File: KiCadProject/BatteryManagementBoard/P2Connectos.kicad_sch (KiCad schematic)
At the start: 25 parts

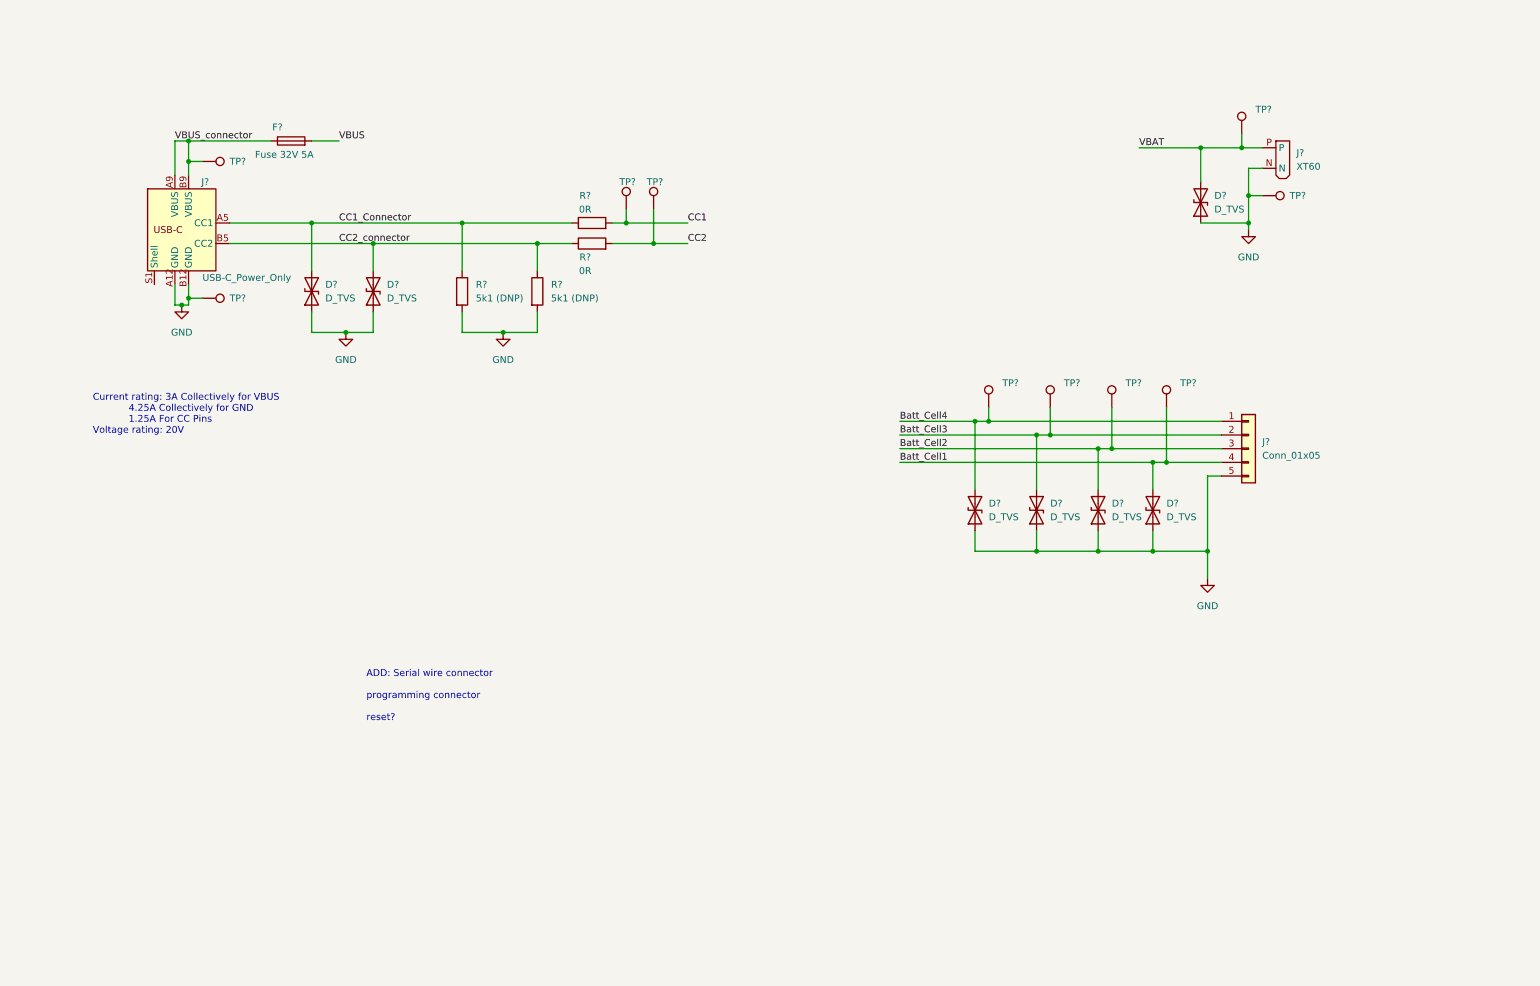
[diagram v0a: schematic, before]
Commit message: BQ25713 layout start
Signed-off-by: Eldalote.Electronics <Eldalote.Electronics@gmail.com>
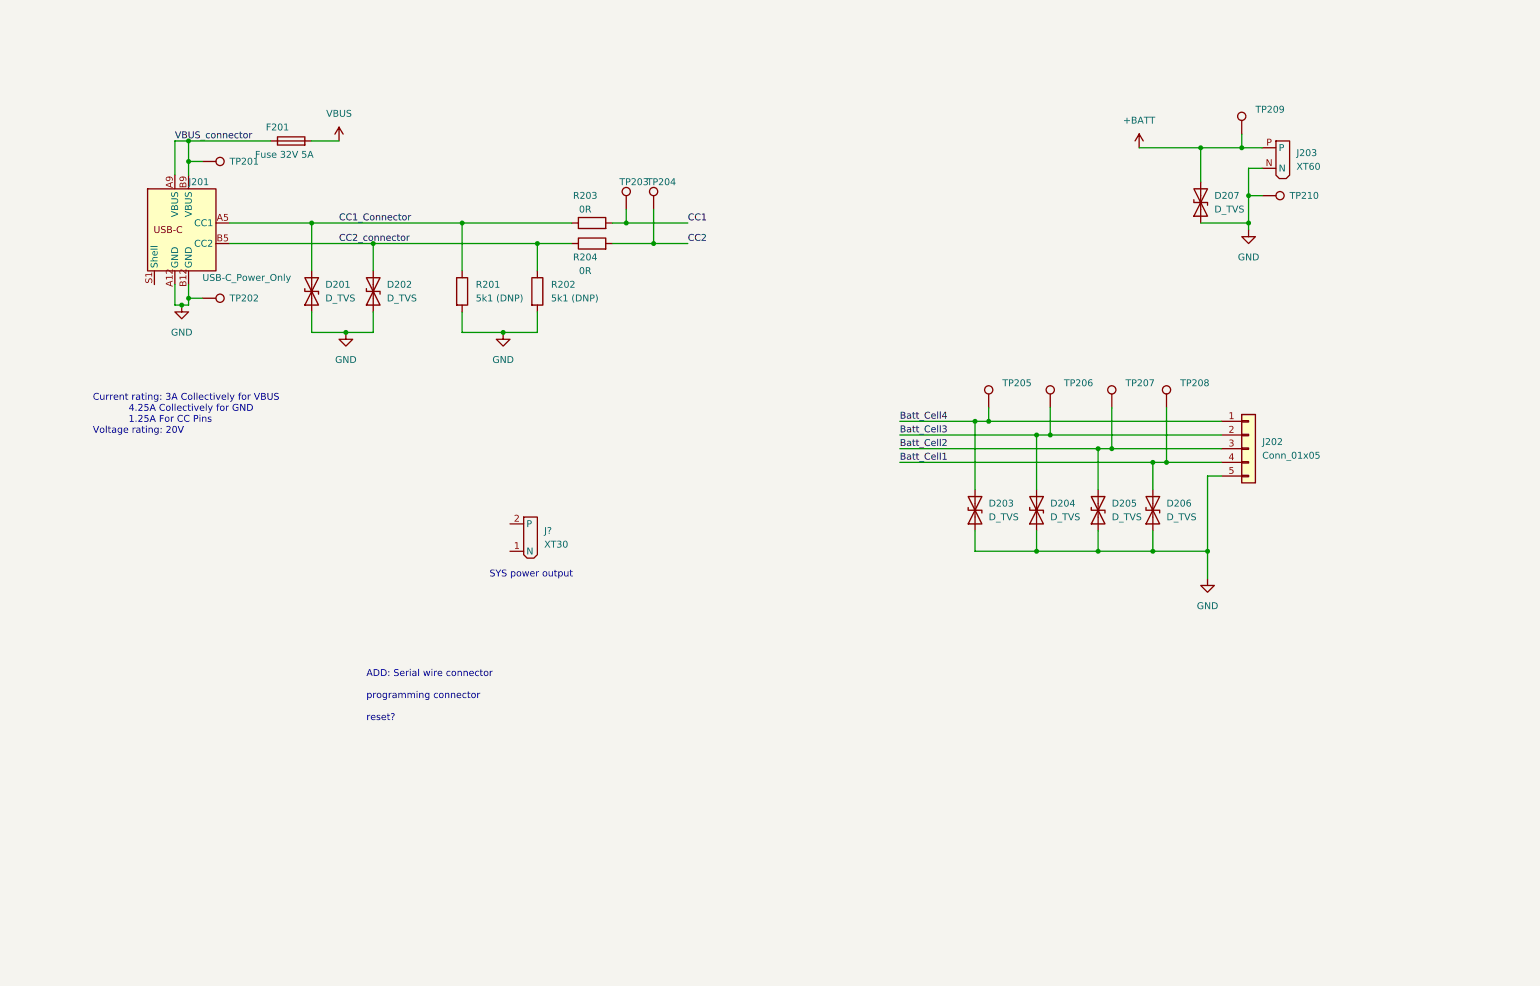
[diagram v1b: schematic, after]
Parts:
- added J?: XT30, Eldalote-footprints:XT30, symbol Eldalote_symbols:XT30
- gave numbers to parts that had none: 25
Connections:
- net VBAT renamed +BATT
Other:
- note added: "SYS power output"

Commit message: BQ25713 and LDO done? Stm32 next I think
Signed-off-by: Eldalote.Electronics <Eldalote.Electronics@gmail.com>
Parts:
- gave numbers to parts that had none: 1
- renumbered J202 to J203, J203 to J204
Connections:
- no-connect marks 0 -> 1
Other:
- note added: "ADD: Serial wire connector programming connector reset? Connector to ESP32"
- note added: "VOUT power output to LED driver"
- note removed: "ADD: Serial wire connector programming connector reset?"
- note removed: "SYS power output"
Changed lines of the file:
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@@
   (junction (at 194.31 91.44) (diameter 0) (color 0 0 0 0)
   )
+  (no_connect (at 39.37 66.04))
   (wire (pts (xy 217.17 88.9) (xy 217.17 96.52))
     (stroke (width 0) (type default) (color 0 0 0 0))
@@
     (stroke (width 0) (type default) (color 0 0 0 0))
   )
-  (text "SYS power output\n" (at 101.6 120.65 0)
-    (effects (font (size 1.27 1.27)) (justify left bottom))
-  )
-  (text "ADD: Serial wire connector\n\nprogramming connector\n\nreset?"
-    (at 78.74 147.32 0)
+  (text "VOUT power output to LED driver\n\n" (at 99.06 121.92 0)
+    (effects (font (size 1.27 1.27)) (justify left bottom))
+  )
+  (text "ADD: Serial wire connector\n\nprogramming connector\n\nreset?\n\nConnector to ESP32\n"
+    (at 55.88 152.4 0)
     (effects (font (size 1.27 1.27)) (justify left bottom))
   )
@@
   (symbol (lib_id "Eldalote_symbols:XT30") (at 107.95 113.03 0) (unit 1)
     (in_bom yes) (on_board yes) (fields_autoplaced)
-    (property "Reference" "J?" (id 0) (at 111.76 111.7599 0)
+    (property "Reference" "J202" (id 0) (at 111.76 111.7599 0)
       (effects (font (size 1.27 1.27)) (justify left))
     )
@@
   (symbol (lib_id "power:VBUS") (at 73.66 39.37 0) (unit 1)
     (in_bom yes) (on_board yes) (fields_autoplaced)
-    (property "Reference" "#PWR?" (id 0) (at 73.66 43.18 0)
+    (property "Reference" "#PWR0202" (id 0) (at 73.66 43.18 0)
       (effects (font (size 1.27 1.27)) hide)
     )
@@
   (symbol (lib_id "power:+BATT") (at 222.25 40.64 0) (unit 1)
     (in_bom yes) (on_board yes) (fields_autoplaced)
-    (property "Reference" "#PWR?" (id 0) (at 222.25 44.45 0)
+    (property "Reference" "#PWR0205" (id 0) (at 222.25 44.45 0)
       (effects (font (size 1.27 1.27)) hide)
     )
@@
   (symbol (lib_id "power:GND") (at 74.93 74.93 0) (unit 1)
     (in_bom yes) (on_board yes) (fields_autoplaced)
-    (property "Reference" "#PWR0202" (id 0) (at 74.93 81.28 0)
+    (property "Reference" "#PWR0203" (id 0) (at 74.93 81.28 0)
       (effects (font (size 1.27 1.27)) hide)
     )
@@
   (symbol (lib_id "Connector_Generic:Conn_01x05") (at 242.57 96.52 0) (unit 1)
     (in_bom yes) (on_board yes) (fields_autoplaced)
-    (property "Reference" "J202" (id 0) (at 245.11 95.2499 0)
+    (property "Reference" "J203" (id 0) (at 245.11 95.2499 0)
       (effects (font (size 1.27 1.27)) (justify left))
     )
@@
   (symbol (lib_id "power:GND") (at 234.95 120.65 0) (unit 1)
     (in_bom yes) (on_board yes) (fields_autoplaced)
-    (property "Reference" "#PWR0204" (id 0) (at 234.95 127 0)
+    (property "Reference" "#PWR0206" (id 0) (at 234.95 127 0)
       (effects (font (size 1.27 1.27)) hide)
     )
@@
   (symbol (lib_id "power:GND") (at 242.57 55.88 0) (unit 1)
     (in_bom yes) (on_board yes) (fields_autoplaced)
-    (property "Reference" "#PWR0205" (id 0) (at 242.57 62.23 0)
+    (property "Reference" "#PWR0207" (id 0) (at 242.57 62.23 0)
       (effects (font (size 1.27 1.27)) hide)
     )
@@
   (symbol (lib_id "power:GND") (at 104.14 74.93 0) (unit 1)
     (in_bom yes) (on_board yes) (fields_autoplaced)
-    (property "Reference" "#PWR0203" (id 0) (at 104.14 81.28 0)
+    (property "Reference" "#PWR0204" (id 0) (at 104.14 81.28 0)
       (effects (font (size 1.27 1.27)) hide)
     )
@@
   (symbol (lib_id "Eldalote_symbols:XT60") (at 247.65 43.18 0) (unit 1)
     (in_bom yes) (on_board yes) (fields_autoplaced)
-    (property "Reference" "J203" (id 0) (at 251.46 41.5924 0)
-      (effects (font (size 1.27 1.27)) (justify left))
-    )
+    (property "Reference" "J204" (id 0) (at 251.46 41.5924 0)
+      (effects (font (size 1.27 1.27)) (justify left))
+    )

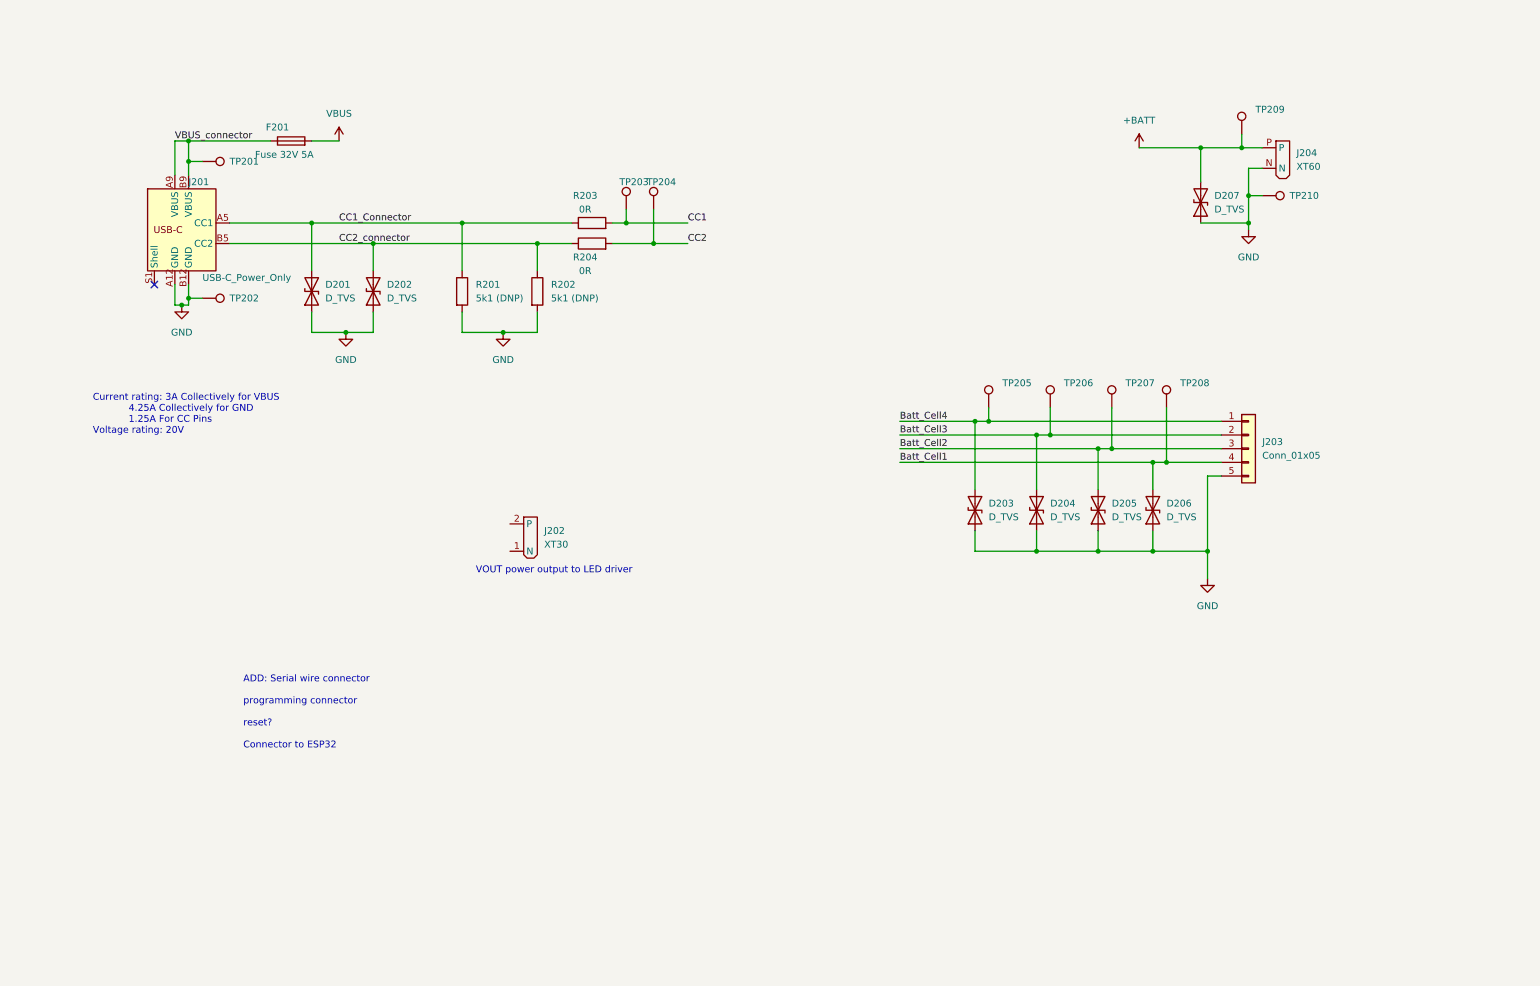
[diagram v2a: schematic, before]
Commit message: Change to design: No more STM32, just use resistors for USB-C PD, en move the battery cell measuring and leveling to the other board.
Signed-off-by: Eldalote.Electronics <Eldalote.Electronics@gmail.com>
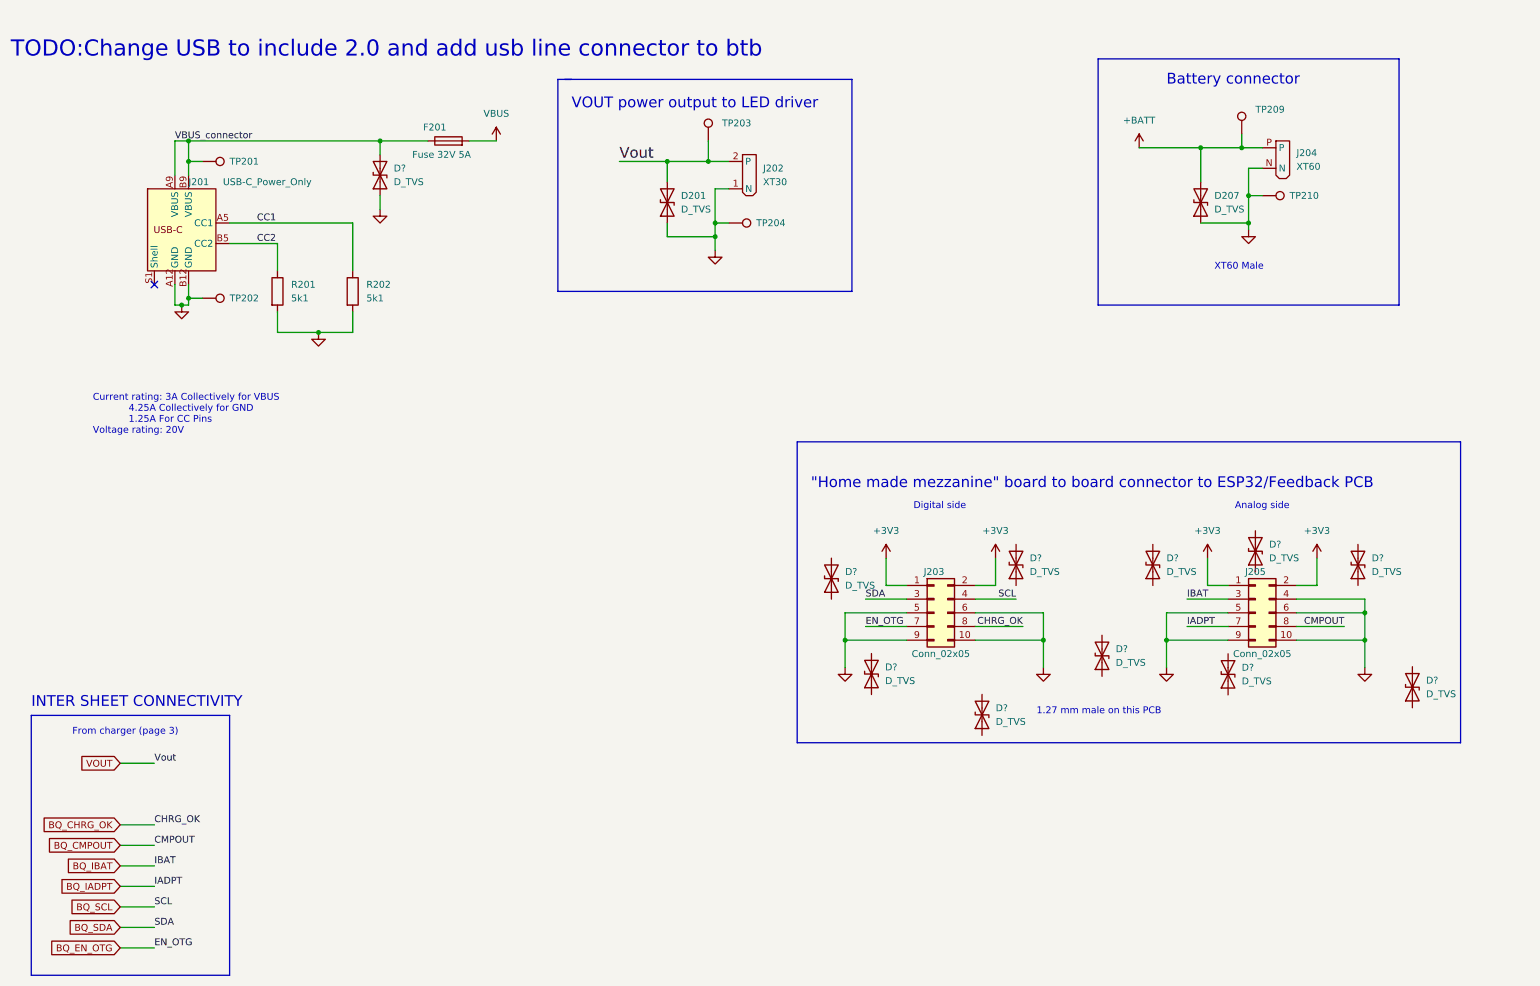
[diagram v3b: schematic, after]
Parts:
- removed D202, D203, D204, D205, D206: D_TVS, symbol Device:D_TVS
- removed J203: Conn_01x05, symbol Connector_Generic:Conn_01x05
- removed R203, R204: 0R, symbol Device:R
- removed TP205, TP206, TP207, TP208: TestPoint, symbol Connector:TestPoint
- added D? (x11): D_TVS, symbol Device:D_TVS
- added J203, J205: Conn_02x05, Connector_PinHeader_1.27mm:PinHeader_2x05_P1.27mm_Vertical_SMD, symbol Connector_Generic:Conn_02x05_Odd_Even
- R201, R202: value 5k1 (DNP) -> 5k1
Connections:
- net CC1: now also J201.A5 (CC1), R202.1; no longer TP203.1
- net CC2: now also J201.B5 (CC2), R201.1; no longer TP204.1
- net GND: now also J202.1 (N), TP204.1, D?.1 (A1), J203.10 (Pin_10), J203.5 (Pin_5), J203.6 (Pin_6), J203.9 (Pin_9), J205.10 (Pin_10), J205.4 (Pin_4), J205.5 (Pin_5), J205.6 (Pin_6), J205.9 (Pin_9)
- net VBUS_connector: now also D?.2 (A2)
- net VOUT: now reaches J202.2 (P)
- net VOUT: now also D201.2 (A2), TP203.1
- removed net CC1_Connector: D201.2 (A2), J201.A5 (CC1), R201.1
- removed net CC2_connector: J201.B5 (CC2), R202.1
- new net +3V3: J203.1 (Pin_1), J203.2 (Pin_2), J205.1 (Pin_1), J205.2 (Pin_2)
- new net BQ_CHRG_OK: J203.8 (Pin_8)
- new net BQ_CMPOUT: J205.8 (Pin_8)
- new net BQ_EN_OTG: J203.7 (Pin_7)
- new net BQ_IADPT: J205.7 (Pin_7)
- new net BQ_IBAT: J205.3 (Pin_3)
- new net BQ_SCL: J203.4 (Pin_4)
- new net BQ_SDA: J203.3 (Pin_3)
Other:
- note added: ""Home made mezzanine" board to board connector to ESP32/Feedback PCB"
- note added: "1.27 mm male on this PCB"
- note added: "Analog side"
- note added: "Battery connector"
- note added: "Digital side"
- note added: "From charger (page 3)"
- note added: "INTER SHEET CONNECTIVITY"
- note added: "TODO:Change USB to include 2.0 and add usb line connector to btb"
- note added: "XT60 Male"
- note removed: "ADD: Serial wire connector programming connector reset? Connector to ESP32"
- company: (none) -> Eldalote Electronics
- moved on the sheet: F201, J202, R201, R202

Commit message: jan 4
Signed-off-by: Eldalote.Electronics <Eldalote.Electronics@gmail.com>
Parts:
- removed D? (x9): D_TVS, symbol Device:D_TVS
- removed J201: USB-C_Power_Only, Imported:USB-C-GCT-USB4140-GF-0170, symbol Eldalote_symbols:USB-C_Power_Only
- added D204, D205, D206, D208, D209, D210, D211, D212, D213: D_TVS, symbol Device:D_TVS
- added J201: USB-C-2.0, Imported:GCT_USB4120-03-C_REVA, symbol Eldalote_symbols:USB-C-2.0
- added J206: Conn_01x02_Male, Connector_PinHeader_1.27mm:PinHeader_1x02_P1.27mm_Vertical, symbol Connector:Conn_01x02_Male
- gave numbers to parts that had none: 2
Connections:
- net BQ_SDA is gone; now on net SDA: J203.3 (Pin_3)
- net +3V3: now also D208.2 (A2), D209.2 (A2)
- net BQ_CHRG_OK: now also D205.2 (A2)
- net BQ_CMPOUT: now also D212.2 (A2)
- net BQ_EN_OTG: now also J205.4 (Pin_4), D213.2 (A2); no longer J203.7 (Pin_7)
- net BQ_IADPT: now also D211.2 (A2)
- net BQ_IBAT: now also D210.2 (A2)
- net CC1: now also J201.A5 (CC1)
- net CC2: now also J201.B5 (CC2)
- net GND: now also D203.1 (A1), D204.1 (A1), D205.1 (A1), D206.1 (A1), D208.1 (A1), D209.1 (A1), D210.1 (A1), D211.1 (A1), D212.1 (A1), D213.1 (A1), J201.A1 (GND), J201.A12 (GND), J201.B1 (GND), J201.B12 (GND); no longer J205.4 (Pin_4)
- net VBUS_connector: now also J201.A4 (VBUS), J201.A9 (VBUS), J201.B4 (VBUS), J201.B9 (VBUS)
- net SDA: now reaches D203.2 (A2)
- net BQ_SCL renamed SCL
- net SCL: now also D206.2 (A2)
- new net: J201.S1 (Shell), J201.S2 (Shell), J201.S3 (Shell), J201.S4 (Shell)
- new net TUS_INT_N: D204.2 (A2), J203.7 (Pin_7)
- new net USB-N: J201.A7 (DN1), J201.B7 (DN2), J206.1 (Pin_1)
- new net USB-P: J201.A6 (DP1), J201.B6 (DP2), J206.2 (Pin_2)
- no-connect marks 1 -> 3
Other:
- note added: "Connector directly to ESP board"
- note added: "Current rating: 5A Collectively for VBUS 6.25A Collectively for GND 1.25A For CC Pins 0.25A For other pins Voltage rating: 20V"
- note added: "I2C to page 3 and 5"
- note added: "To/From USB-PD controller (page 5)"
- note added: "When the USB PD controller is not used (default) use pull down resistors. When the USB PD controller is to be used, replace pull down resistors with TVS diode"
- note removed: "Current rating: 3A Collectively for VBUS 4.25A Collectively for GND 1.25A For CC Pins Voltage rating: 20V"
- note removed: "TODO:Change USB to include 2.0 and add usb line connector to btb"
- moved on the sheet: D203, J203, R201, R202, TP201, TP202
